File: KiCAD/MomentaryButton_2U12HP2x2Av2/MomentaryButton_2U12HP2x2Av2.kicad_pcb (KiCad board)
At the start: 2 copper layers, 60.6 x 84 mm, 8 parts, among them SW1 SW_SPST_M16_Panel_Mount_Push-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, SW2 SW_SPST_M16_Panel_Mount_Push-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, SW3 SW_SPST_M16_Panel_Mount_Push-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, SW4 SW_SPST_M16_Panel_Mount_Push-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

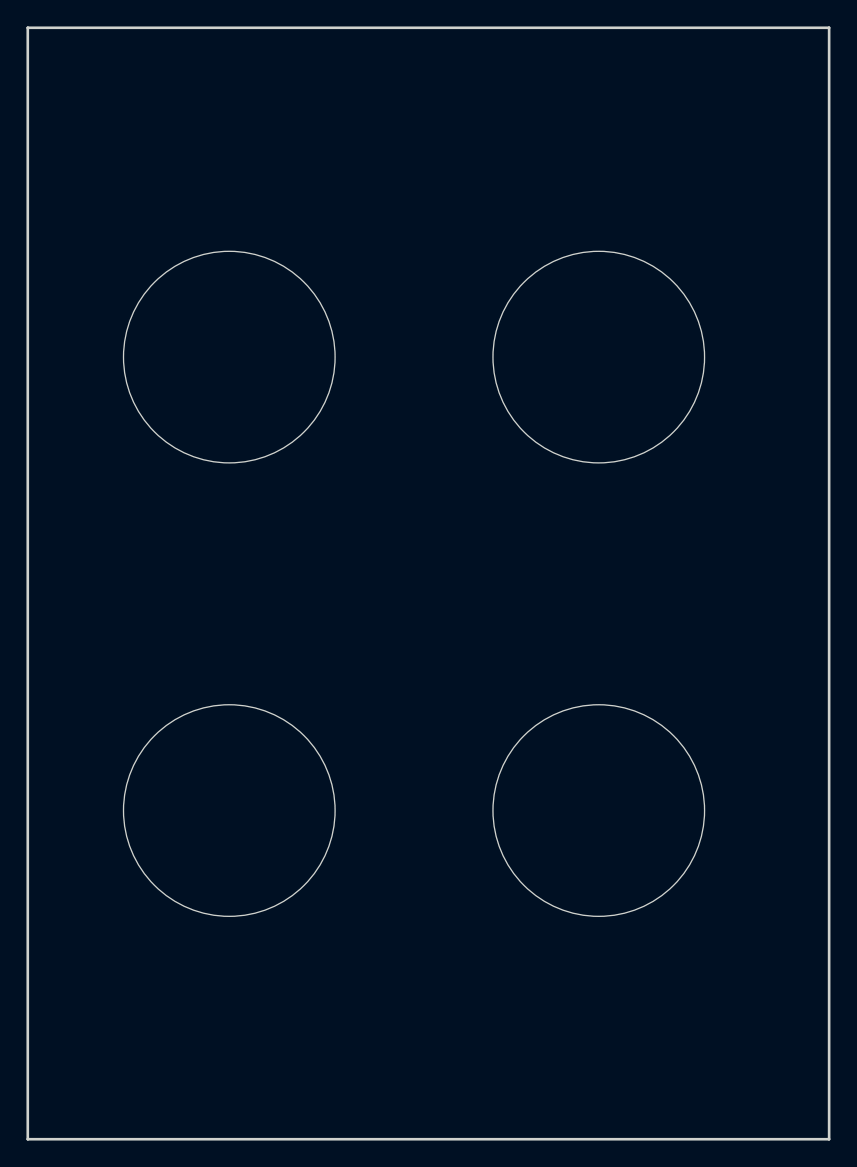
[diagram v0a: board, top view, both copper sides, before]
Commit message: updated all modules to use plated through-holes wherever possible
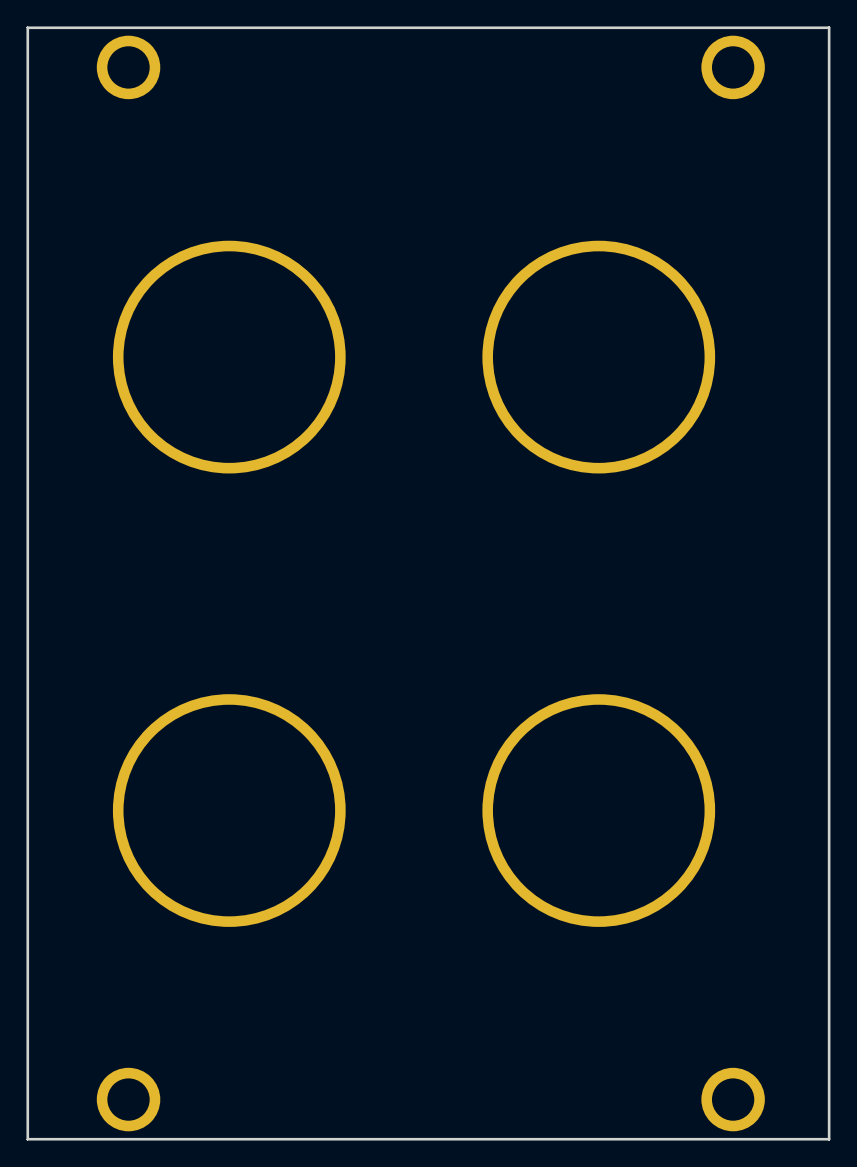
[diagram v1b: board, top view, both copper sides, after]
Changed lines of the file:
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@@
 			)
 		)
-		(pad "" np_thru_hole oval
+		(pad "" thru_hole circle
 			(at 0 0)
-			(size 4.34 3.2)
-			(drill oval 4.34 3.2)
+			(size 4.8 4.8)
+			(drill 3.2)
 			(layers "*.Cu" "*.Mask")
+			(remove_unused_layers no)
 		)
 		(embedded_fonts no)
@@
 			)
 		)
-		(pad "" np_thru_hole oval
+		(pad "" thru_hole circle
 			(at 0 0)
-			(size 4.34 3.2)
-			(drill oval 4.34 3.2)
+			(size 4.8 4.8)
+			(drill 3.2)
 			(layers "*.Cu" "*.Mask")
+			(remove_unused_layers no)
 		)
 		(embedded_fonts no)
@@
 			)
 		)
-		(pad "" np_thru_hole circle
+		(pad "" thru_hole circle
 			(at 0 0)
-			(size 16 16)
+			(size 17.6 17.6)
 			(drill 16)
 			(layers "*.Cu" "*.Mask")
+			(remove_unused_layers no)
 		)
 		(embedded_fonts no)
@@
 			)
 		)
-		(pad "" np_thru_hole circle
+		(pad "" thru_hole circle
 			(at 0 0)
-			(size 16 16)
+			(size 17.6 17.6)
 			(drill 16)
 			(layers "*.Cu" "*.Mask")
+			(remove_unused_layers no)
 		)
 		(embedded_fonts no)
@@
 			)
 		)
-		(pad "" np_thru_hole oval
+		(pad "" thru_hole circle
 			(at 0 0)
-			(size 4.34 3.2)
-			(drill oval 4.34 3.2)
+			(size 4.8 4.8)
+			(drill 3.2)
 			(layers "*.Cu" "*.Mask")
+			(remove_unused_layers no)
 		)
 		(embedded_fonts no)
@@
 			)
 		)
-		(pad "" np_thru_hole oval
+		(pad "" thru_hole circle
 			(at 0 0)
-			(size 4.34 3.2)
-			(drill oval 4.34 3.2)
+			(size 4.8 4.8)
+			(drill 3.2)
 			(layers "*.Cu" "*.Mask")
+			(remove_unused_layers no)
 		)
 		(embedded_fonts no)
@@
 			)
 		)
-		(pad "" np_thru_hole circle
+		(pad "" thru_hole circle
 			(at 0 0)
-			(size 16 16)
+			(size 17.6 17.6)
 			(drill 16)
 			(layers "*.Cu" "*.Mask")
+			(remove_unused_layers no)
 		)
 		(embedded_fonts no)
@@
 			)
 		)
-		(pad "" np_thru_hole circle
+		(pad "" thru_hole circle
 			(at 0 0)
-			(size 16 16)
+			(size 17.6 17.6)
 			(drill 16)
 			(layers "*.Cu" "*.Mask")
+			(remove_unused_layers no)
 		)
 		(embedded_fonts no)
